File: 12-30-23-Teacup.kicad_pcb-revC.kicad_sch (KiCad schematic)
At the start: 102 parts, among them IC1 T31ZX, J1 USB Type-C, J10 AudioJack4_Ground, J11 Conn_01x04_Pin, J12 Conn_01x04_Pin, J13 SFW15R-2STE1LF, J2 Micro_SD_Card, J3 USB_A, J4 Conn_02x08_Odd_Even, J5 UART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

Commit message: Update 12-30-23-Teacup.kicad_pcb-revC.kicad_sch
Update schematic
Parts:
- removed R22, R23: 100k, Resistor_SMD:R_0603_1608Metric_Pad0.98x0.95mm_HandSolder, symbol Device:R
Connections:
- net +2V8 is gone; now on net PA15: J4.1 (Pin_1)
- net +3V3: now also J13.5
- net GND: no longer J4.3 (Pin_3)
- net at R13.2, U4.3 (IO2): now also U5.3 (IO2)
- net at U5.7 (IO3): now also R14.1, U4.7 (IO3)
- net CAM_PE renamed PA18
- net PA18: now also J4.3 (Pin_3); no longer J13.5
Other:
- moved on the sheet: C23

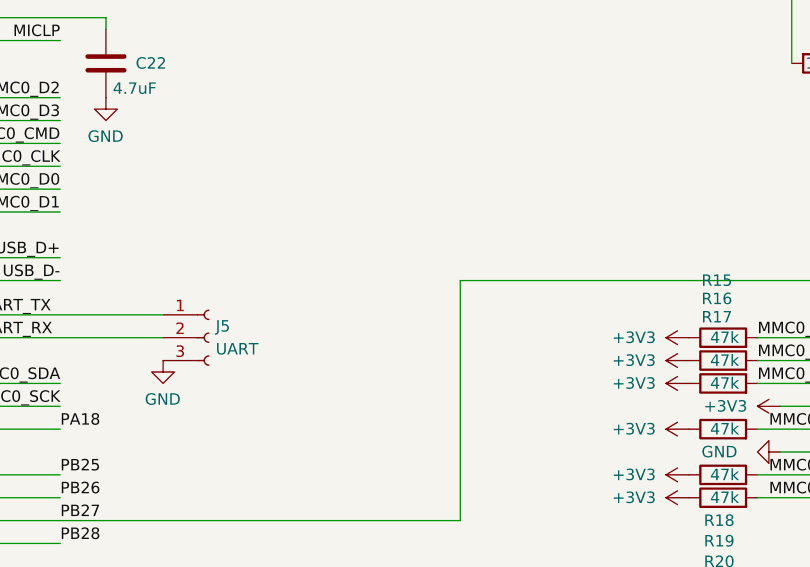
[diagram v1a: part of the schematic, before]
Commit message: Added R22 pullup resistor on PB27 to help the card detect recognition on the SD card
Added R22 pullup resistor on PB27 to help the card detect recognition on the SD card
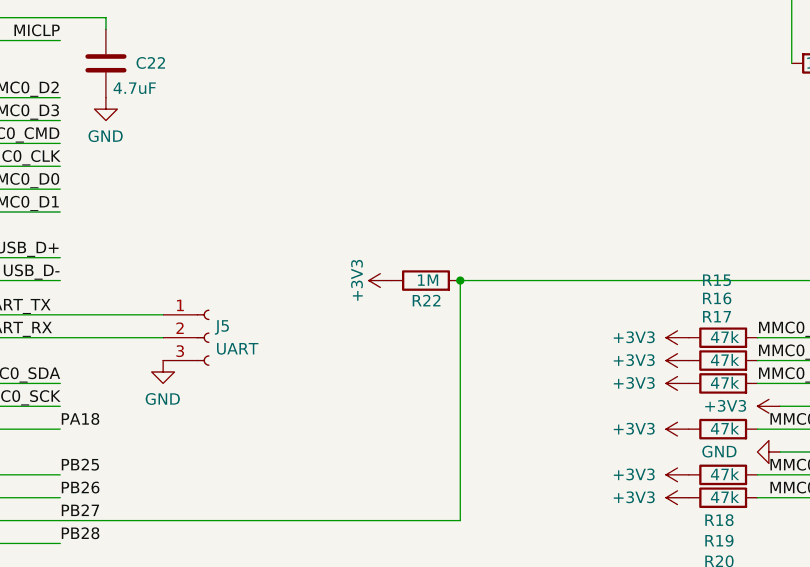
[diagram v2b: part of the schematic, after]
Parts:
- added R22: 1M, Resistor_SMD:R_0402_1005Metric, symbol Device:R
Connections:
- net +3V3: now also R22.1
- net PB27: now also R22.2

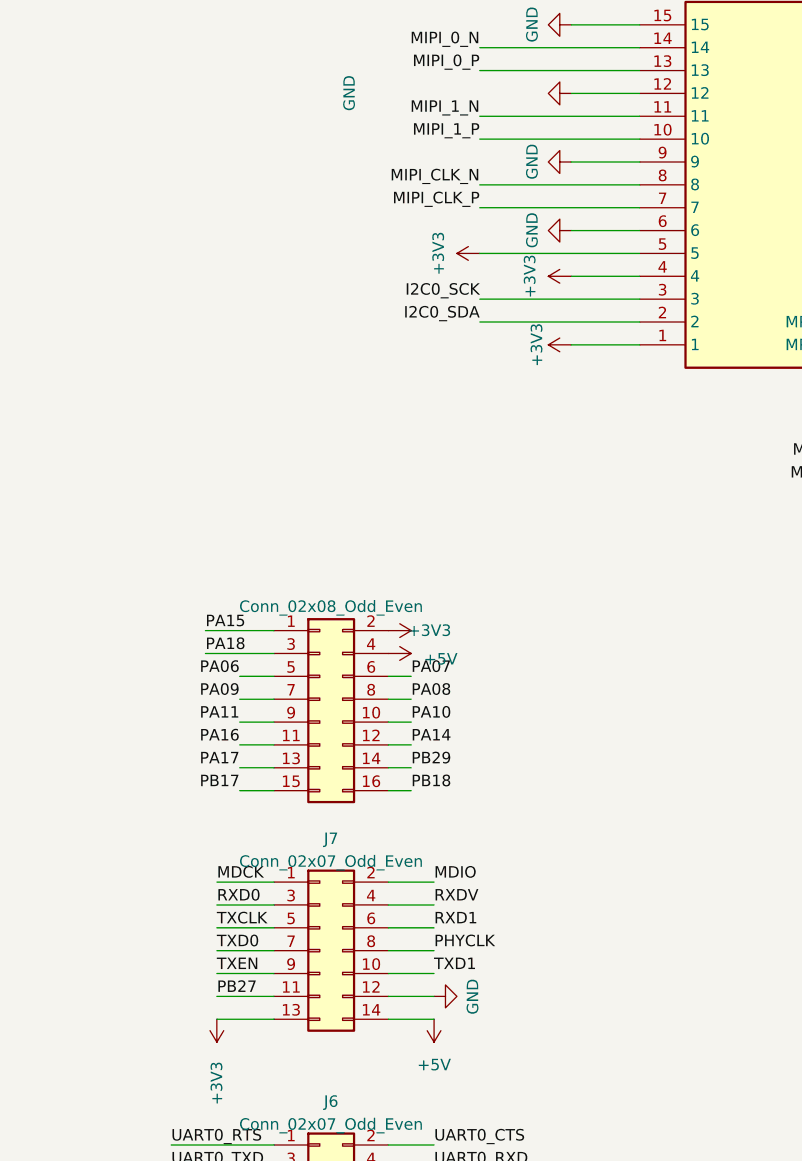
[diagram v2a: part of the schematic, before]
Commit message: Update silkscreen labels, add solder jumper for sensor enable
Update silkscreen labels, add solder jumper for sensor enable
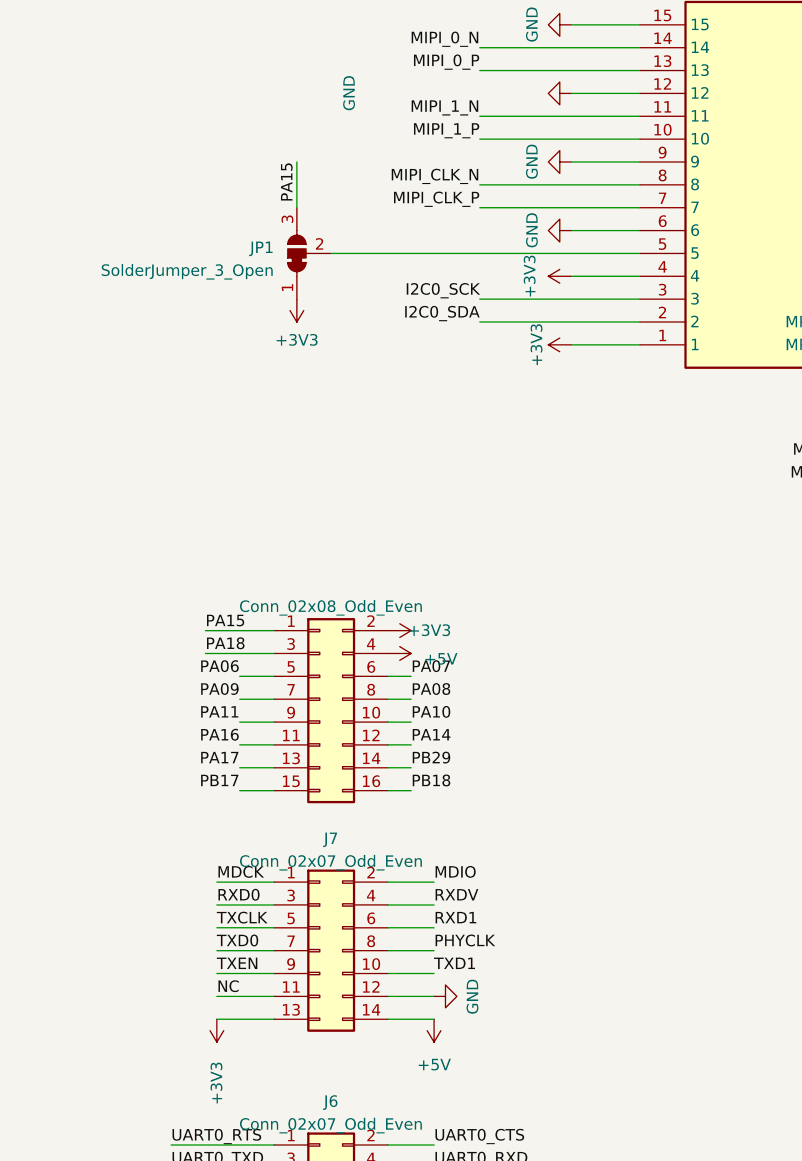
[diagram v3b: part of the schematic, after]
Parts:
- added JP1: SolderJumper_3_Open, Jumper:SolderJumper-3_P1.3mm_Bridged12_Pad1.0x1.5mm, symbol Jumper:SolderJumper_3_Bridged12
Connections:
- net +3V3: now also JP1.1 (A); no longer J13.5
- net PA15: now also JP1.3 (B)
- net PB27: no longer J7.11 (Pin_11)
- new net: J13.5, JP1.2 (C)
- new net NC: J7.11 (Pin_11)
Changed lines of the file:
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@@
     (stroke (width 0) (type default))
   )
+  (wire (pts (xy 31.75 123.19) (xy 31.75 128.27))
+    (stroke (width 0) (type default))
+  )
   (wire (pts (xy 195.58 132.08) (xy 198.12 132.08))
     (stroke (width 0) (type default))
@@
     (stroke (width 0) (type default))
   )
-  (wire (pts (xy 52.07 133.35) (xy 69.85 133.35))
+  (wire (pts (xy 35.56 133.35) (xy 69.85 133.35))
     (stroke (width 0) (type default))
   )
@@
     (effects (font (size 1.27 1.27)) (justify right bottom))
   )
+  (label "PA15" (at 31.75 123.19 270) (fields_autoplaced)
+    (effects (font (size 1.27 1.27)) (justify right bottom))
+  )
   (label "PB29" (at 243.84 240.03 0) (fields_autoplaced)
     (effects (font (size 1.27 1.27)) (justify left bottom))
@@
     (effects (font (size 1.27 1.27)) (justify left bottom))
   )
-  (label "PB27" (at 22.86 215.9 0) (fields_autoplaced)
+  (label "NC" (at 22.86 215.9 0) (fields_autoplaced)
     (effects (font (size 1.27 1.27)) (justify left bottom))
   )
@@
     )
   )
-  (symbol (lib_id "power:+3V3") (at 52.07 133.35 90) (unit 1)
-    (in_bom yes) (on_board yes) (dnp no)
-    (property "Reference" "#PWR045" (at 55.88 133.35 0)
-      (effects (font (size 1.27 1.27)) hide)
-    )
-    (property "Value" "+3V3" (at 47.498 133.35 0)
-      (effects (font (size 1.27 1.27)))
-    )
-    (property "Footprint" "" (at 52.07 133.35 0)
-      (effects (font (size 1.27 1.27)) hide)
-    )
-    (property "Datasheet" "" (at 52.07 133.35 0)
-      (effects (font (size 1.27 1.27)) hide)
-    )
-    (pin "1")
-    (instances
-      (project "12-30-23-Teacup.kicad_pcb-revC"
-        (path "/6e7ef4e6-2026-4726-8de0-60238113f775"
-          (reference "#PWR045") (unit 1)
-        )
-      )
-    )
-  )
   (symbol (lib_id "power:+3V3") (at 229.87 125.73 0) (unit 1)
     (in_bom yes) (on_board yes) (dnp no)
@@
     )
   )
+  (symbol (lib_id "Jumper:SolderJumper_3_Bridged12") (at 31.75 133.35 90) (unit 1)
+    (in_bom yes) (on_board yes) (dnp no) (fields_autoplaced)
+    (property "Reference" "JP1" (at 29.21 132.715 90)
+      (effects (font (size 1.27 1.27)) (justify left))
+    )
+    (property "Value" "SolderJumper_3_Open" (at 29.21 135.255 90)
+      (effects (font (size 1.27 1.27)) (justify left))
+    )
+    (property "Footprint" "Jumper:SolderJumper-3_P1.3mm_Bridged12_Pad1.0x1.5mm" (at 31.75 133.35 0)
+      (effects (font (size 1.27 1.27)) hide)
+    )
+    (property "Datasheet" "~" (at 31.75 133.35 0)
+      (effects (font (size 1.27 1.27)) hide)
+    )
+    (pin "1")
+    (pin "2")
+    (pin "3")
+    (instances
+      (project "12-30-23-Teacup.kicad_pcb-revC"
+        (path "/6e7ef4e6-2026-4726-8de0-60238113f775"
+          (reference "JP1") (unit 1)
+        )
+      )
+    )
+  )
   (symbol (lib_id "power:+3V3") (at 279.4 205.74 90) (mirror x) (unit 1)
     (in_bom yes) (on_board yes) (dnp no)
@@
         )
       )
+    )
+  )
+  (symbol (lib_id "power:+3V3") (at 31.75 138.43 180) (unit 1)
+    (in_bom yes) (on_board yes) (dnp no)
+    (property "Reference" "#PWR045" (at 31.75 134.62 0)
+      (effects (font (size 1.27 1.27)) hide)
+    )
+    (property "Value" "+3V3" (at 31.75 143.002 0)
+      (effects (font (size 1.27 1.27)))
+    )
+    (property "Footprint" "" (at 31.75 138.43 0)
+      (effects (font (size 1.27 1.27)) hide)
+    )
+    (property "Datasheet" "" (at 31.75 138.43 0)
+      (effects (font (size 1.27 1.27)) hide)
+    )
+    (pin "1")
+    (instances
+      (project "12-30-23-Teacup.kicad_pcb-revC"
+        (path "/6e7ef4e6-2026-4726-8de0-60238113f775"
+          (reference "#PWR045") (unit 1)
+        )
+      )
